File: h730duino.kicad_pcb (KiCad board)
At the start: 4 copper layers, 101.6 x 53.3 mm, 112 parts, among them J1 USB_C_Receptacle_USB2.0, J2 USB_B_Micro, J3 L834-1G1T-91, J4 105162-0001, J5 Conn_ARM_JTAG_SWD_10, J6 Conn_ARM_JTAG_SWD_10, J7 Conn_02x03_Odd_Even, P1 CONN_02x18, P10 CONN_01X01, P11 CONN_01X01, P13 CONN_01X01, P2 CONN_01x08, P3 CONN_01x08, P4 CONN_01x08, P5 CONN_01x10, P6 CONN_01x08, P7 CONN_01x08, P8 CONN_01X01, SW1 RESET, U1 STM32H730ZBT6, U10 LY68L6400SLI, U12 AP2161W, U2 IS25LP032D-JBLE-TR, U3 TPS62162DSG, U4 TPS62163DSG, U5 MAX40200AUK, U6 MAX40200AUK, U7 STM32F042F6Px, U8 MAX40200AUK, U9 KSZ8081RNA, Y1 32.768K, Y2 8M, Y3 25M

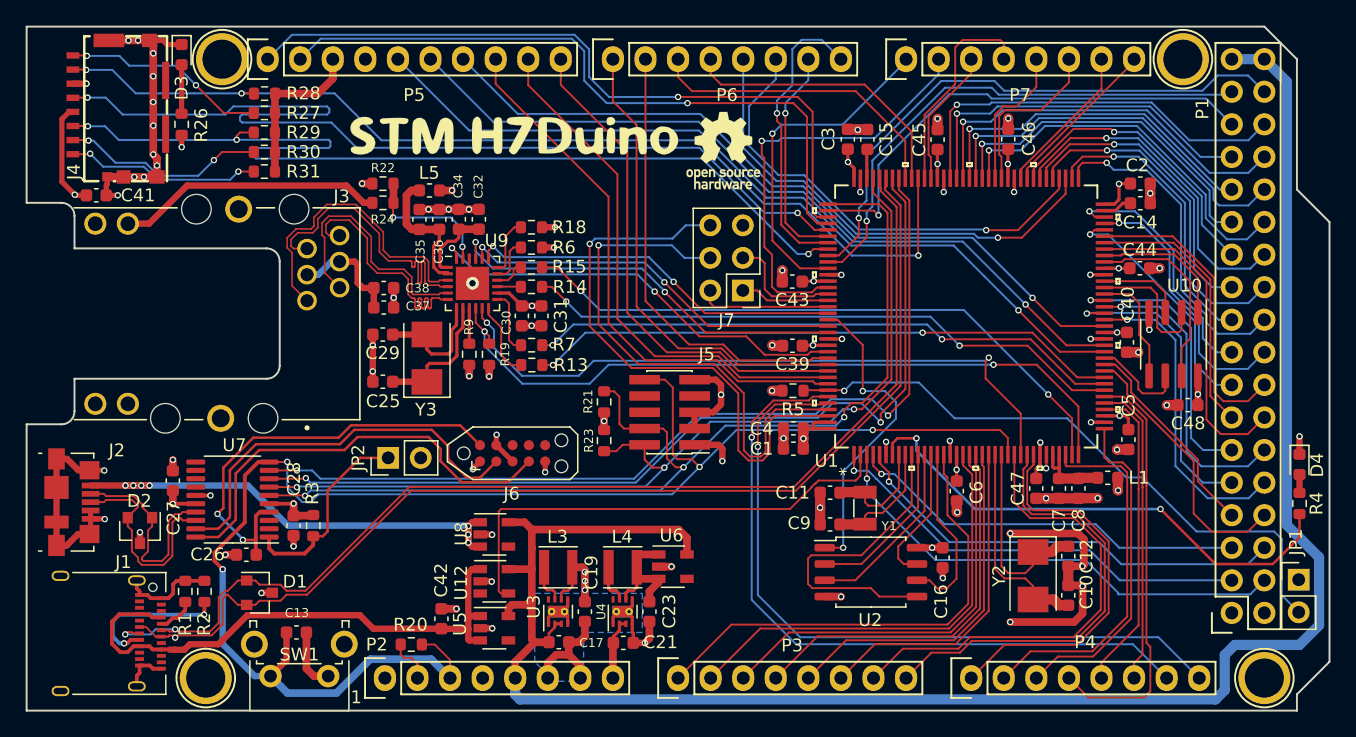
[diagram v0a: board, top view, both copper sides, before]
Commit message: Replace STM32F042 in TSSOP by STM32F04[28] in QFN28
Others changes:

 - Export gerbers to current status
 - Update schematic export in svg and pdf
 - Update README image
 - Rename `USB OTG` sheet to `USB_OTG`

Signed-off-by: Martin Ribelotta <martinribelotta@gmail.com>
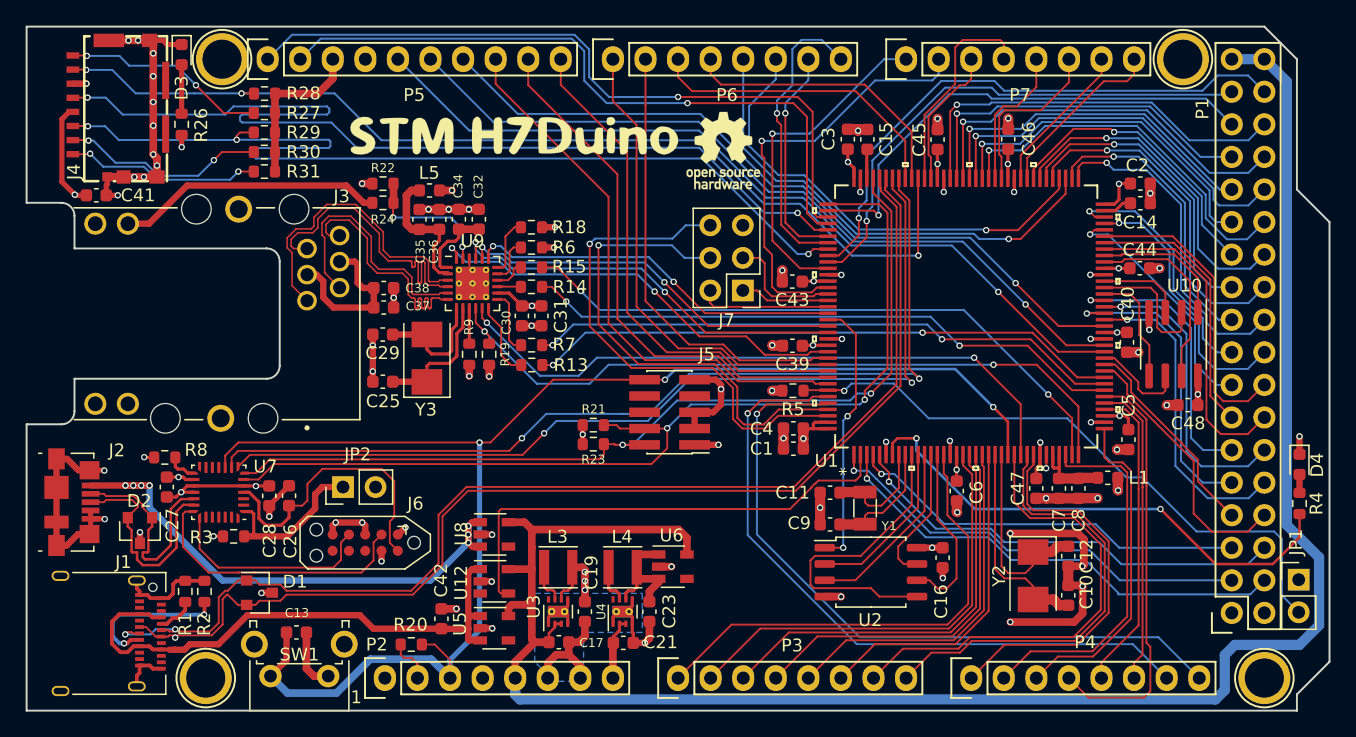
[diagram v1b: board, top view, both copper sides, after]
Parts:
- added R8: 10K, Resistor_SMD:R_0603_1608Metric, F.Cu at (114.2, 101.9)
- U7: value STM32F042F6Px -> STM32F048G6Ux; footprint Package_SO:TSSOP-20_4.4x6.5mm_P0.65mm -> Package_DFN_QFN:QFN-28_4x4mm_P0.5mm
- U9: footprint Package_DFN_QFN:QFN-24-1EP_4x4mm_P0.5mm_EP2.6x2.6mm -> Package_DFN_QFN:QFN-24-1EP_4x4mm_P0.5mm_EP2.6x2.6mm_ThermalVias
- moved J6 13.4 mm to (129.8, 108.6), turned to 180 degrees
- moved R3 6.26 mm to (119.5, 108.1), turned to 0 degrees
- moved C26 5.69 mm to (123.8, 104.9), turned to 90 degrees
- moved JP2 4.19 mm to (128.0, 104.2)
- moved C28 3.00 mm to (122.3, 104.9)
- moved R21 2.00 mm to (147.6, 99.4), turned to 0 degrees
- moved U7 1.21 mm to (118.4, 104.6)
- moved R23 0.89 mm to (147.6, 100.9), turned to 0 degrees
- moved C27 0.69 mm to (114.3, 104.2)
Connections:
- U7 pad 15: GND -> Net-(R8-Pad2)
- U7 pad 16: +3V3 -> GND
- U7 pad 17: /Debug/USBD_D- -> +3V3
- U7 pad 18: /Debug/USBD_D+ -> +3V3
- U7 pad 19: /Debug/DBG_SWDIO -> /Debug/USBD_D-
- U7 pad 20: /Debug/DBG_SWCK -> /Debug/USBD_D+
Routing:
- net /Debug/DBG_SWCK: track 34.0 -> 16.5 mm
- net /Debug/~DBGR: track 33.9 -> 22.9 mm, vias 2 -> 0
- net /Debug/DBG_SWDIO: track 31.4 -> 21.8 mm
- net /~RST: track 119.9 -> 112.6 mm, vias 4 -> 3
- net /EXT0: track 44.9 -> 40.1 mm
- net /EXT1: track 43.0 -> 38.3 mm
- net Net-(C37-Pad2): track 8.84 -> 12.9 mm
- net /DBG_VBUS: track 37.3 -> 41.4 mm
- net /SWCLK: track 81.2 -> 77.2 mm, vias 3 -> 2
- net GND: track 169.8 -> 173.3 mm, vias 73 -> 71
- net /OCTOSPIM_P2_NCS: track 24.6 -> 21.1 mm
- net /SWDIO: track 74.6 -> 71.7 mm, vias 3 -> 2
- net /USART1_TX: track 71.2 -> 73.9 mm
- net /Debug/DBGB: track 15.7 -> 13.1 mm
- net +3V3: track 89.6 -> 92.0 mm, vias 31 -> 33
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
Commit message: Save point
Signed-off-by: Martin Ribelotta <martinribelotta@gmail.com>
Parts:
- added R10: 10K, Resistor_SMD:R_0603_1608Metric, F.Cu at (133.4, 104.4)
- moved C35 1.80 mm to (132.8, 84.7)
- moved C36 1.80 mm to (134.4, 84.7)
- moved L5 1.49 mm to (134.2, 82.4), turned to 0 degrees
- moved C32 0.68 mm to (138.0, 83.2)
- moved C34 0.68 mm to (136.4, 83.2)
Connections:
- C38 pad 1: Net-(C37-Pad2) -> Net-(C38-Pad1)
- J3 pad 11: Net-(C37-Pad2) -> Net-(C38-Pad1)
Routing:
- net /Debug/~DBGR: track 22.9 -> 29.0 mm
- net Net-(C37-Pad2): track 12.9 -> 7.01 mm
- net Net-(C38-Pad1): track 0.00 -> 3.85 mm
- net Net-(R22-Pad1): track 10.8 -> 14.1 mm, vias 2 -> 0
- net /Debug/DBG_SWCK: track 16.5 -> 13.9 mm
- net Net-(C35-Pad1): track 10.6 -> 8.34 mm
- net GND: track 173.3 -> 171.8 mm, vias 71 -> 70
- net /Debug/DBG_SWDIO: track 21.8 -> 20.8 mm
- net +3V3: track 92.0 -> 91.1 mm
- net /ETH_TXD1: track 32.0 -> 31.3 mm

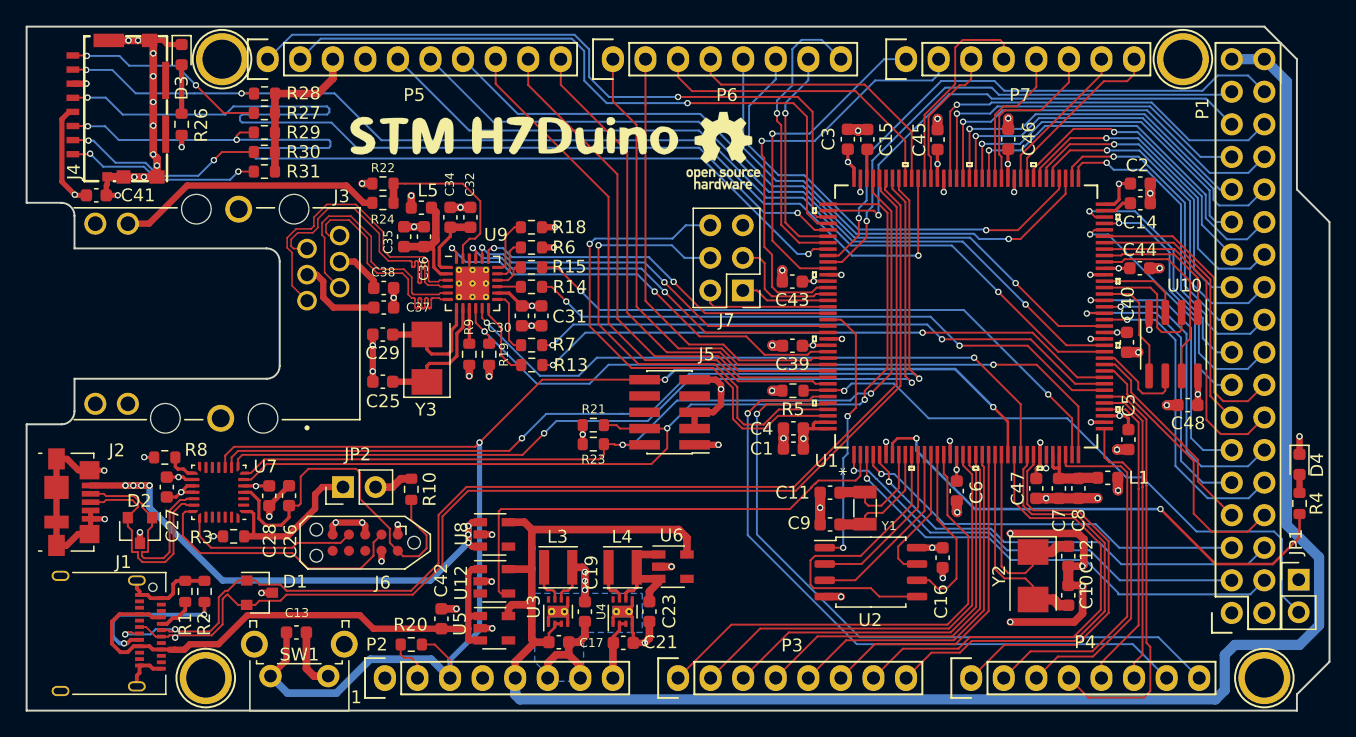
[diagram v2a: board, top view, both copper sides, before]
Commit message: Change QSPI PSRAM to hyperRAM
 - Replace QSPI PSRAM to HyperBUS version due to erratasheet
   of mcu (cannot write in QSPI mode without DQS and DQS not
   work in 4bit mode)
 - Connect hyperram to QSPI interface 2
 - Move QSPI flash to interface 1
 - Rearrangue pinouts due to new functionality
 - Remove extra pinouts (now all pins are in arduino connector9
 - Improve schematic and libreries to pass ERC
 - Add pin-1 mark on all IC

Signed-off-by: Martin Ribelotta <martinribelotta@gmail.com>
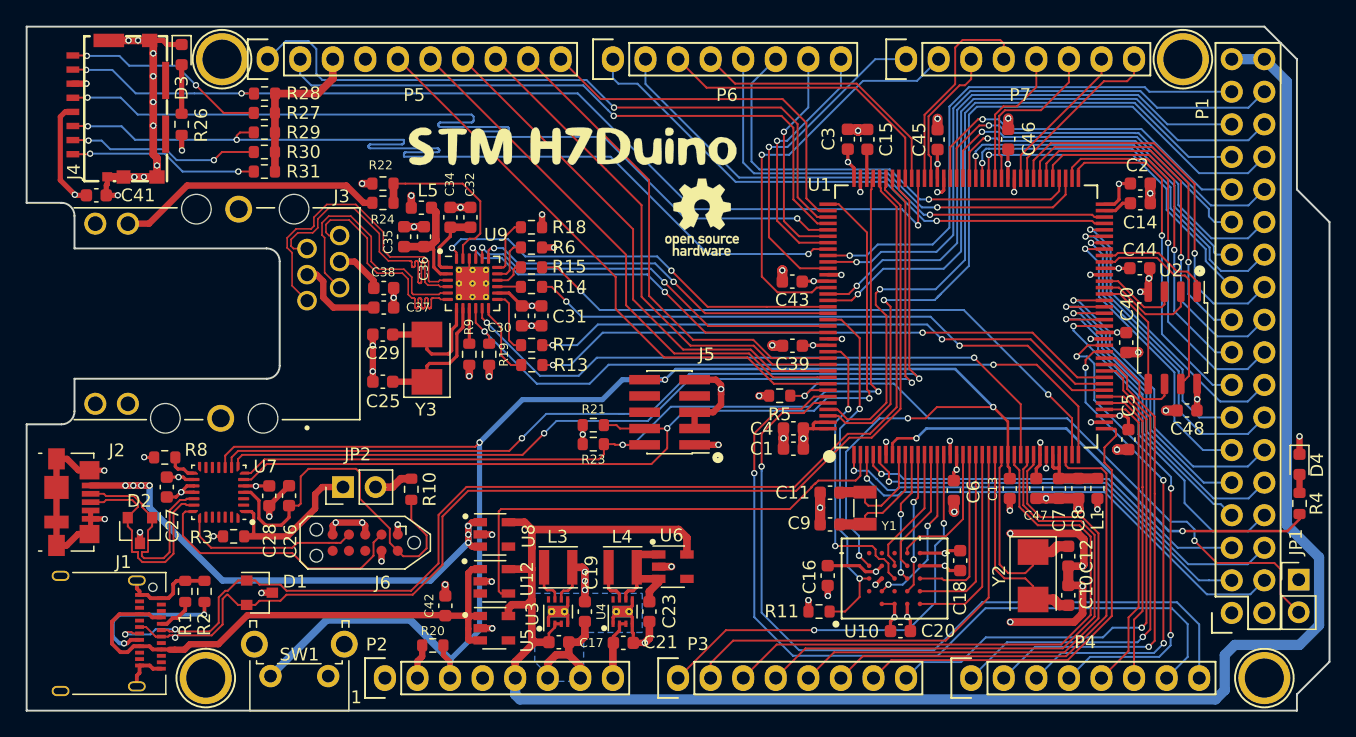
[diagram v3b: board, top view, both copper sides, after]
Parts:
- removed J7: Conn_02x03_Odd_Even, Connector_PinHeader_2.54mm:PinHeader_2x03_P2.54mm_Vertical
- added C18: 100n, Capacitor_SMD:C_0603_1608Metric, F.Cu at (176.2, 110.0)
- added C20: 100n, Capacitor_SMD:C_0603_1608Metric, F.Cu at (171.5, 115.5)
- added R11: 10K, Resistor_SMD:R_0603_1608Metric, F.Cu at (165.2, 113.9)
- U10: value LY68L6400SLI -> S27KL0641DABHI020; footprint Package_SO:SOIC-8_3.9x4.9mm_P1.27mm -> footprints:S27KL0641DABHI020
- moved C13 56.7 mm to (180.0, 104.3), turned to 270 degrees
- moved U2 29.8 mm to (192.7, 92.6), turned to 270 degrees
- moved U10 28.4 mm to (171.1, 111.4), turned to 90 degrees
- moved C16 9.07 mm to (165.8, 111.1)
- moved LOGO1 5.45 mm to (156.0, 83.2)
- moved G1 4.64 mm to (146.0, 77.6)
- moved R20 1.68 mm to (135.1, 116.6)
- moved L1 1.16 mm to (186.9, 104.3), turned to 90 degrees
- moved R5 1.11 mm to (162.1, 97.1)
- moved C42 1.06 mm to (136.0, 113.5)
- moved C48 0.42 mm to (193.9, 98.3)
- moved C6 0.23 mm to (175.7, 104.5)
- moved C40 0.06 mm to (189.1, 93.0)
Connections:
- U1 pad 110: /24 -> /8(**)
- U1 pad 117: /23 -> /22
- U1 pad 118: /22 -> /23
- U1 pad 123: /EXT4 -> /24
- U1 pad 124: /EXT3 -> /25
- U1 pad 125: /EXT2 -> /~ETH_RST
- U1 pad 132: /~ETH_RST -> /OCTOSPIM_P2_DQS
- U1 pad 133: /6(**) -> /9(**)
- U1 pad 134: /7(**) -> /10(**)
- U1 pad 135: /8(**) -> /11(**)
- U1 pad 136: /9(**) -> /12(**)
- U1 pad 137: /10(**) -> /13(**)
- U1 pad 141: /EXT1 -> /26
- U1 pad 142: /EXT0 -> /27
- U1 pad 18: /A1 -> /OCTOSPIM_P1_IO3
- U1 pad 19: /A2 -> /OCTOSPIM_P1_IO2
- U1 pad 20: /A3 -> /OCTOSPIM_P1_IO0
- U1 pad 21: /A4 -> /OCTOSPIM_P1_IO1
- U1 pad 22: /A5 -> /A1
- U1 pad 26: /A6 -> /A2
- U1 pad 28: /A7 -> /A3
- U1 pad 29: /A8 -> /A4
- U1 pad 34: /A9 -> /A5
- U1 pad 37: /A10 -> /A6
- U1 pad 42: /A11 -> /A7
- U1 pad 46: /49 -> /A8
- U1 pad 47: /48 -> /A9
- U1 pad 49: /13(**) -> /A10
- U1 pad 50: /12(**) -> /A11
- U1 pad 53: /11(**) -> /49
- U1 pad 54: /47 -> /48
- U1 pad 55: /46 -> /47
- U1 pad 56: /45 -> /46
- U1 pad 57: /44 -> /45
- U1 pad 65: /43 -> /44
- U1 pad 66: /42 -> /43
- U1 pad 67: /41 -> /42
- U1 pad 68: /40 -> /41
- U1 pad 69: /39 -> /7(**)
- U1 pad 70: /38 -> /6(**)
- U1 pad 73: /37 -> /40
- U1 pad 74: /36 -> /39
- U1 pad 77: /35 -> /38
- U1 pad 78: /34 -> /37
- U1 pad 79: /33 -> /36
- U1 pad 80: /32 -> /35
- U1 pad 87: /31 -> /34
- U1 pad 88: /30 -> /33
- U1 pad 89: /29 -> /32
- U1 pad 90: /28 -> /31
- U1 pad 91: /27 -> /30
- U1 pad 92: /26 -> /29
- U1 pad 93: /25 -> /28
- U2 pad 1: /OCTOSPIM_P2_NCS -> /OCTOSPIM_P1_NCS
- U2 pad 2: /OCTOSPIM_P2_IO1 -> /OCTOSPIM_P1_IO5
- U2 pad 3: /OCTOSPIM_P2_IO2 -> /OCTOSPIM_P1_IO6
- U2 pad 5: /OCTOSPIM_P2_IO0 -> /OCTOSPIM_P1_IO4
- U2 pad 6: /OCTOSPIM_P2_CLK -> /OCTOSPIM_P1_CLK
- U2 pad 7: /OCTOSPIM_P2_IO3 -> /OCTOSPIM_P1_IO7
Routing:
- net /EXT0: track 40.1 -> 0.00 mm, vias 1 -> 0
- net /EXT1: track 38.3 -> 0.00 mm, vias 1 -> 0
- net /27: track 30.8 -> 60.1 mm
- net /26: track 28.4 -> 56.6 mm
- net /OCTOSPIM_P2_DQS: track 0.00 -> 23.2 mm, vias 0 -> 2
- net /~RST: track 112.6 -> 134.3 mm, vias 3 -> 5
- net /13(**): track 64.5 -> 45.5 mm, vias 1 -> 0
- net /12(**): track 61.8 -> 43.6 mm, vias 1 -> 0
- net /25: track 31.7 -> 48.8 mm
- net /11(**): track 58.6 -> 41.7 mm, vias 1 -> 0
- net /OCTOSPIM_P1_IO1: track 0.00 -> 15.7 mm
- net /OCTOSPIM_P1_IO0: track 0.00 -> 14.6 mm
- net /OCTOSPIM_P2_IO0: track 24.2 -> 10.2 mm, vias 0 -> 2
- net /A4: track 28.1 -> 41.7 mm
- net /OCTOSPIM_P1_IO2: track 0.00 -> 13.5 mm
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
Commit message: Return to lan8742A in ETH PHY
Signed-off-by: Martin Ribelotta <martinribelotta@gmail.com>
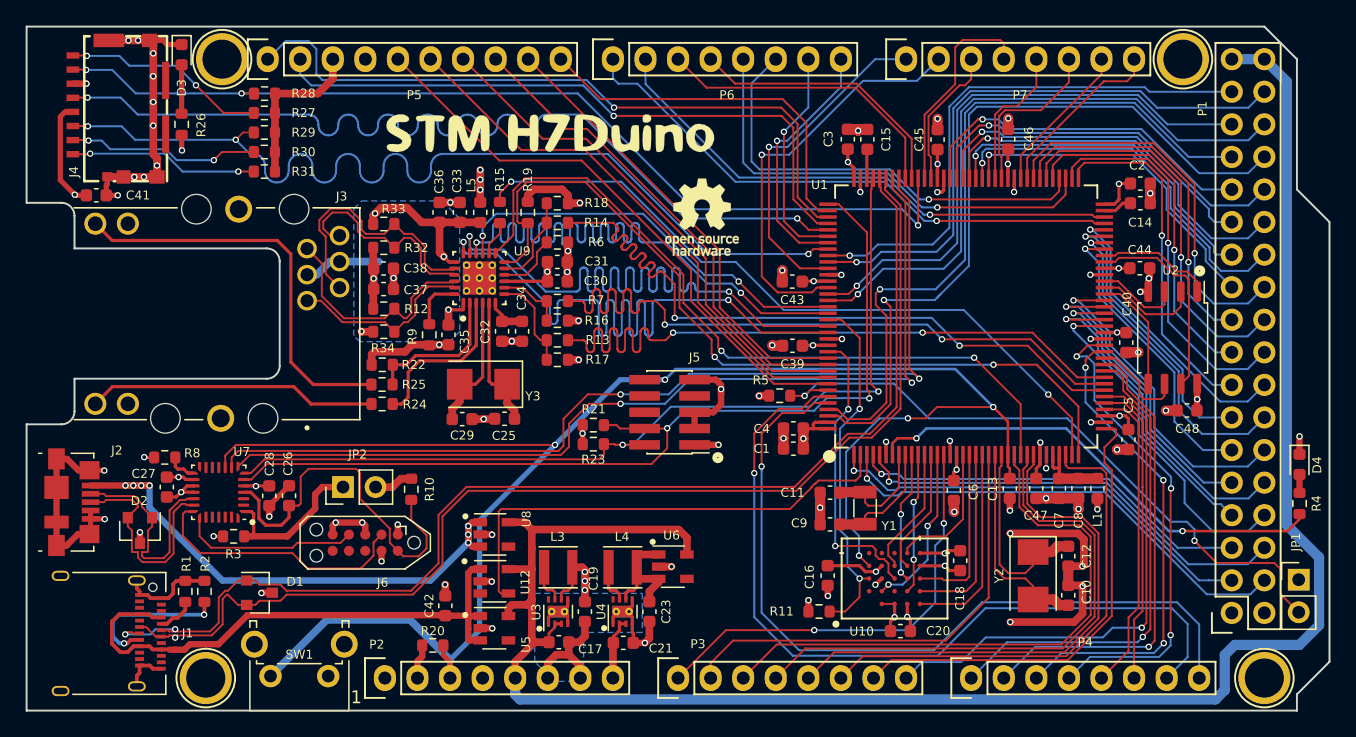
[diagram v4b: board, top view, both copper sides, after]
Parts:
- added C33: 100n, Capacitor_SMD:C_0603_1608Metric, F.Cu at (137.2, 82.8)
- added R12: 49.9R, Resistor_SMD:R_0603_1608Metric, F.Cu at (131.2, 90.3)
- added R16: 10K, Resistor_SMD:R_0603_1608Metric, F.Cu at (144.8, 91.3)
- added R17: 10K, Resistor_SMD:R_0603_1608Metric, F.Cu at (144.8, 94.3)
- added R25: 220R, Resistor_SMD:R_0603_1608Metric, F.Cu at (131.1, 96.2)
- added R32: 49.9R, Resistor_SMD:R_0603_1608Metric, F.Cu at (131.2, 85.6)
- added R33: 49.9R, Resistor_SMD:R_0603_1608Metric, F.Cu at (131.2, 83.7)
- added R34: 49.9R, Resistor_SMD:R_0603_1608Metric, F.Cu at (131.2, 92.1)
- C30, C36: value 22u -> 10u
- C32: value 2.2u -> 470p
- C37, C38: value 100n -> 0.022u
- R18: value 1K5 -> 10K
- R9: value 6.49K 1% -> 12.1K 1%
- U9: value KSZ8081RNA -> LAN8742A; footprint Package_DFN_QFN:QFN-24-1EP_4x4mm_P0.5mm_EP2.6x2.6mm_ThermalVias -> footprints:Microchip-C04-143B-S4QFN-0-0-MFG
- moved R24 15.7 mm to (131.1, 97.8)
- moved R22 14.1 mm to (131.1, 94.7), turned to 0 degrees
- moved R19 11.5 mm to (142.5, 82.8)
- moved C34 10.5 mm to (142.0, 92.1), turned to 270 degrees
- moved C25 9.92 mm to (140.6, 98.9)
- moved C32 9.23 mm to (140.5, 92.1), turned to 270 degrees
- moved C29 9.05 mm to (137.3, 98.9), turned to 180 degrees
- moved C35 8.40 mm to (136.3, 92.4), turned to 270 degrees
- moved R14 5.39 mm to (144.8, 83.6)
- moved R15 4.93 mm to (140.3, 82.8), turned to 90 degrees
- moved Y3 4.85 mm to (139.0, 96.2), turned to 180 degrees
- moved L5 4.60 mm to (138.8, 82.8), turned to 270 degrees
- moved C31 4.38 mm to (144.8, 86.7), turned to 0 degrees
- moved R7 3.98 mm to (144.8, 89.7)
- moved C30 3.85 mm to (144.8, 88.2), turned to 0 degrees
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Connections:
- C35 pad 1: Net-(C35-Pad1) -> Net-(C33-Pad1)
- C36 pad 1: Net-(C35-Pad1) -> Net-(C33-Pad1)
- C37 pad 1: GND -> Net-(C33-Pad1)
- C37 pad 2: Net-(C37-Pad2) -> GND
- C38 pad 1: Net-(C38-Pad1) -> Net-(C33-Pad1)
- J3 pad 11: Net-(C38-Pad1) -> Net-(C33-Pad1)
- J3 pad 13: (no net) -> GND
- J3 pad 14: (no net) -> Net-(J3-Pad14)
- J3 pad 15: Net-(J3-Pad15) -> GND
- J3 pad 16: +3V3 -> Net-(J3-Pad16)
- J3 pad 4: /Ethernet/RX_N -> /Ethernet/RX_P
- J3 pad 5: Net-(C37-Pad2) -> Net-(C33-Pad1)
- J3 pad 6: /Ethernet/RX_P -> /Ethernet/RX_N
- L5 pad 2: Net-(C35-Pad1) -> Net-(C33-Pad1)
- R18 pad 2: Net-(R18-Pad2) -> Net-(R14-Pad1)
- R19 pad 1: /ETH_MDIO -> +3V3
- R19 pad 2: +3V3 -> /ETH_MDIO
- R22 pad 1: Net-(R22-Pad1) -> GND
- R22 pad 2: +3V3 -> /Ethernet/LED2
- R24 pad 1: Net-(R22-Pad1) -> /Ethernet/LED1
- R24 pad 2: Net-(J3-Pad15) -> Net-(J3-Pad14)
- R7 pad 1: Net-(R7-Pad1) -> Net-(R16-Pad2)
- U9 pad 1: Net-(C32-Pad1) -> Net-(C33-Pad1)
- U9 pad 10: /ETH_MDIO -> Net-(R6-Pad2)
- U9 pad 11: /ETH_MDC -> Net-(R14-Pad1)
- U9 pad 12: Net-(R13-Pad1) -> /ETH_MDIO
- U9 pad 13: Net-(R7-Pad1) -> /ETH_MDC
- U9 pad 14: +3V3 -> Net-(R15-Pad1)
- U9 pad 15: Net-(R14-Pad1) -> /~ETH_RST
- U9 pad 16: Net-(R15-Pad1) -> /ETH_TX_EN
- U9 pad 17: Net-(R6-Pad2) -> /ETH_TXD0
- U9 pad 18: Net-(R18-Pad2) -> /ETH_TXD1
- U9 pad 19: /ETH_TX_EN -> Net-(C33-Pad1)
- U9 pad 2: Net-(C35-Pad1) -> /Ethernet/LED2
- U9 pad 20: /ETH_TXD0 -> /Ethernet/TX_N
- U9 pad 21: /ETH_TXD1 -> /Ethernet/TX_P
- U9 pad 22: GND -> /Ethernet/RX_N
- U9 pad 23: Net-(R22-Pad1) -> /Ethernet/RX_P
- U9 pad 24: /~ETH_RST -> Net-(R9-Pad1)
- U9 pad 3: /Ethernet/RX_N -> /Ethernet/LED1
- U9 pad 4: /Ethernet/RX_P -> Net-(C29-Pad2)
- U9 pad 5: /Ethernet/TX_N -> Net-(C25-Pad2)
- U9 pad 6: /Ethernet/TX_P -> Net-(C32-Pad1)
- U9 pad 7: Net-(C29-Pad2) -> Net-(R13-Pad1)
- U9 pad 8: Net-(C25-Pad2) -> Net-(R16-Pad2)
- U9 pad 9: Net-(R9-Pad1) -> +3V3
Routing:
- net Net-(J3-Pad16): track 0.00 -> 31.7 mm
- net Net-(C33-Pad1): track 0.00 -> 28.1 mm, vias 0 -> 5
- net /ETH_TX_EN: track 29.3 -> 56.2 mm
- net /ETH_TXD0: track 30.4 -> 56.2 mm
- net /ETH_TXD1: track 31.3 -> 56.2 mm
- net Net-(J3-Pad14): track 0.00 -> 22.7 mm
- net Net-(J3-Pad15): track 20.9 -> 0.00 mm
- net Net-(R22-Pad1): track 14.1 -> 0.00 mm
- net /Ethernet/LED1: track 0.00 -> 12.9 mm
- net /Ethernet/LED2: track 0.00 -> 11.4 mm
- net /ETH_RXD1: track 46.3 -> 56.2 mm
- net /ETH_RXD0: track 46.4 -> 56.2 mm
- net /Ethernet/RX_P: track 23.8 -> 14.7 mm
- net /ETH_CRS_DV: track 47.2 -> 56.2 mm
- net Net-(C35-Pad1): track 8.34 -> 0.00 mm
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- added copper zone on B.Cu, net Net-(C33-Pad1)
